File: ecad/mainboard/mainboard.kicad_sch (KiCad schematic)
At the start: 29 parts, among them M1 Left Motor, M2 Right Motor, Q1 IRLB8721PBF, Q2 IRLB8721PBF, U1 LM339

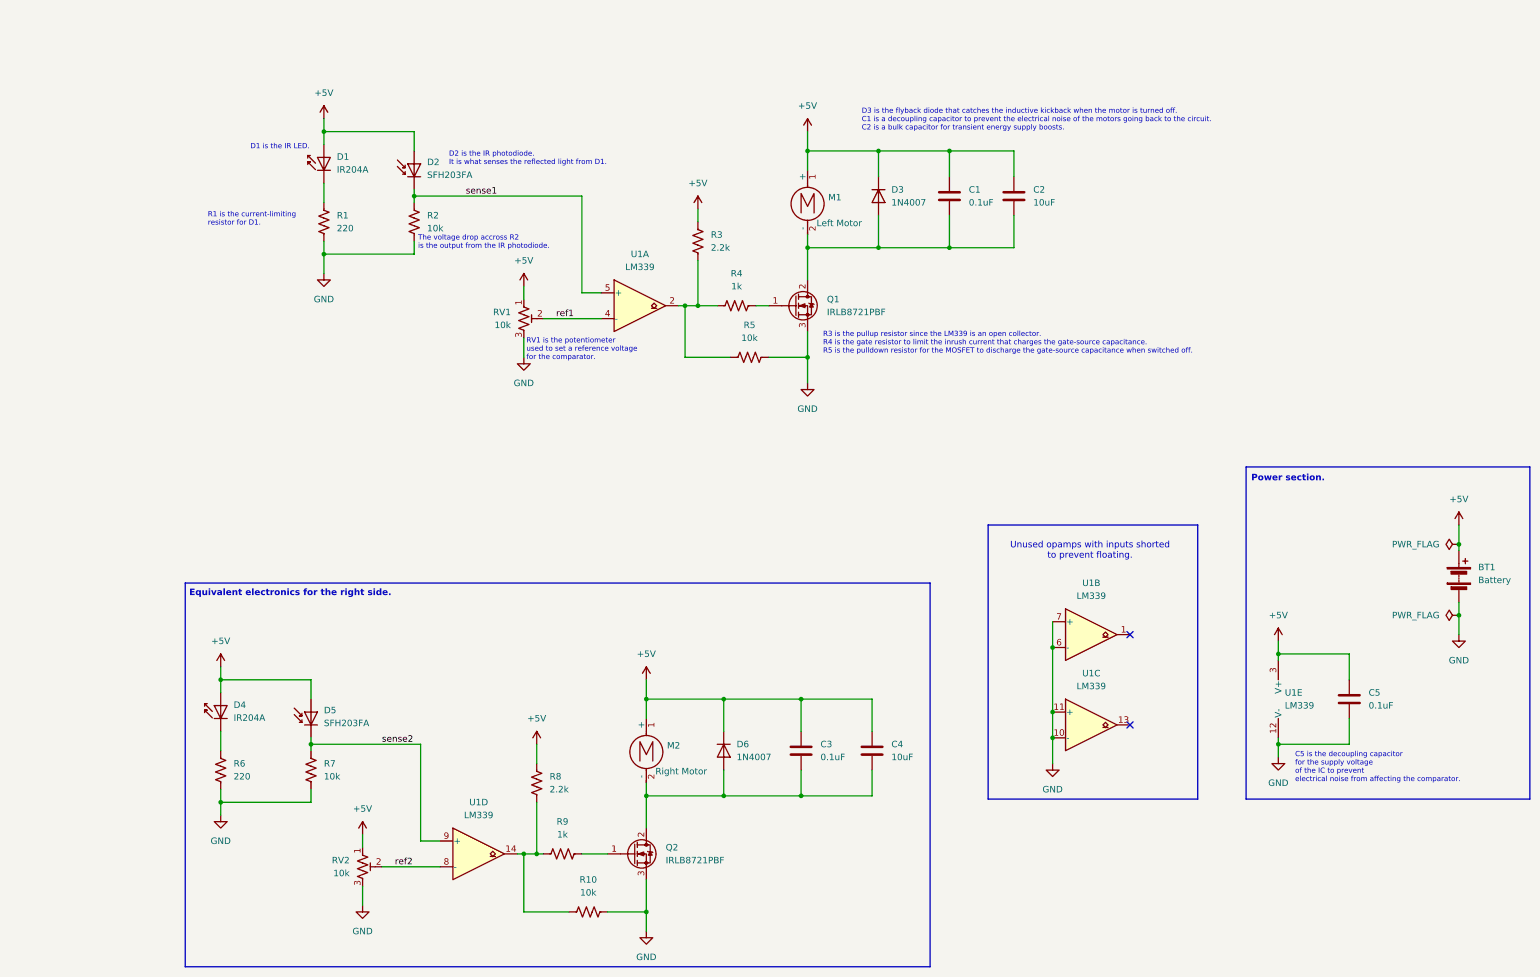
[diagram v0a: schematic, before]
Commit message: update schematics with smd components
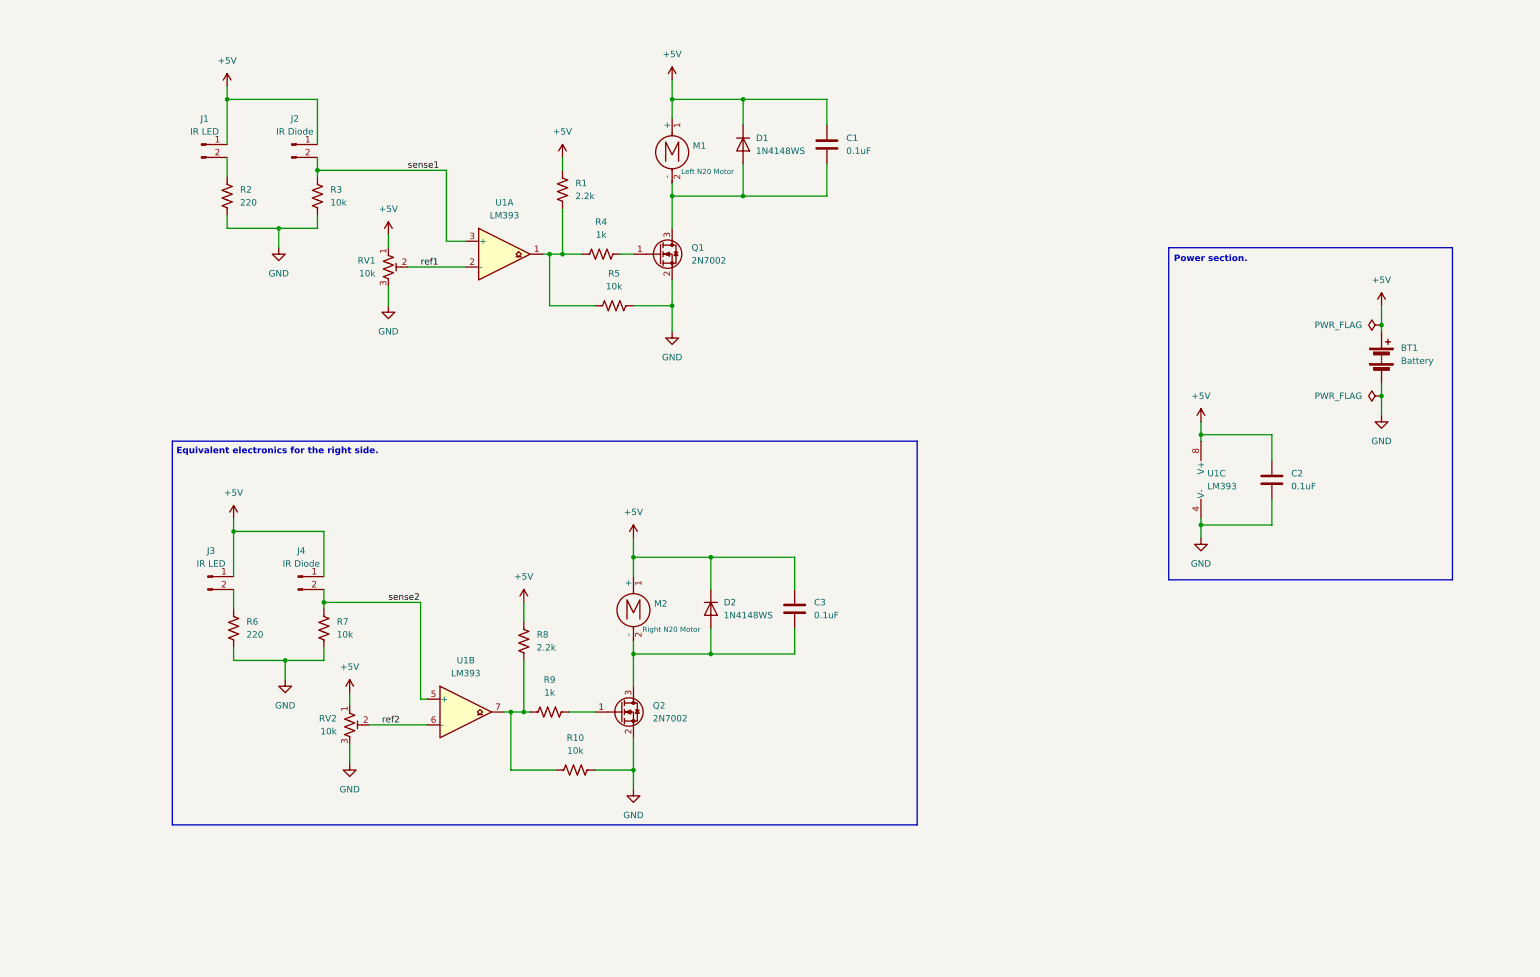
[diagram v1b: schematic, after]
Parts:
- removed C2, C4: 10uF, symbol Device:C
- removed D1, D4: IR204A, LED_THT:LED_D3.0mm_IRBlack, symbol LED:IR204A
- removed D2, D5: SFH203FA, LED_THT:LED_D5.0mm_IRGrey, symbol Sensor_Optical:SFH203FA
- removed Q1, Q2: IRLB8721PBF, Package_TO_SOT_THT:TO-220-3_Vertical, symbol Transistor_FET:IRLB8721PBF
- removed U1: LM339, symbol Comparator:LM339
- added J1, J3: IR LED, Connector_JST:JST_XH_S2B-XH-A_1x02_P2.50mm_Horizontal, symbol Connector:Conn_01x02_Pin
- added J2, J4: IR Diode, Connector_JST:JST_XH_S2B-XH-A_1x02_P2.50mm_Horizontal, symbol Connector:Conn_01x02_Pin
- added Q1, Q2: 2N7002, Package_TO_SOT_SMD:SOT-23, symbol Transistor_FET:2N7002
- added U1: LM393, Package_SO:SOIC-8_3.9x4.9mm_P1.27mm, symbol Comparator:LM393
- C1, C3: footprint (none) -> Capacitor_SMD:C_0402_1005Metric
- C2: renamed from C5; footprint (none) -> Capacitor_SMD:C_0402_1005Metric
- D1: renamed from D3; value 1N4007 -> 1N4148WS; footprint Diode_THT:D_DO-41_SOD81_P10.16mm_Horizontal -> Diode_SMD:D_SOD-323; symbol Diode:1N4007 -> Diode:1N4148WS
- D2: renamed from D6; value 1N4007 -> 1N4148WS; footprint Diode_THT:D_DO-41_SOD81_P10.16mm_Horizontal -> Diode_SMD:D_SOD-323; symbol Diode:1N4007 -> Diode:1N4148WS
- M1: value Left Motor -> Left N20 Motor; footprint Connector_PinHeader_2.54mm:PinHeader_1x02_P2.54mm_Vertical -> Connector_JST:JST_ZH_B2B-ZR_1x02_P1.50mm_Vertical
- M2: value Right Motor -> Right N20 Motor; footprint Connector_PinHeader_2.54mm:PinHeader_1x02_P2.54mm_Vertical -> Connector_JST:JST_ZH_B2B-ZR_1x02_P1.50mm_Vertical
- R1: renamed from R3; footprint Resistor_THT:R_Axial_DIN0309_L9.0mm_D3.2mm_P2.54mm_Vertical -> Resistor_SMD:R_0603_1608Metric
- R10, R4, R5, R6, R7, R8, R9: footprint Resistor_THT:R_Axial_DIN0309_L9.0mm_D3.2mm_P2.54mm_Vertical -> Resistor_SMD:R_0603_1608Metric
- R2: renamed from R1; footprint Resistor_THT:R_Axial_DIN0309_L9.0mm_D3.2mm_P2.54mm_Vertical -> Resistor_SMD:R_0603_1608Metric
- R3: renamed from R2; footprint Resistor_THT:R_Axial_DIN0309_L9.0mm_D3.2mm_P2.54mm_Vertical -> Resistor_SMD:R_0603_1608Metric
- RV1, RV2: footprint Potentiometer_SMD:Potentiometer_Bourns_3214J_Horizontal -> Potentiometer_THT:Potentiometer_Bourns_3296W_Vertical
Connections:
- net +5V: now also J1.1 (Pin_1), J2.1 (Pin_1), J3.1 (Pin_1), J4.1 (Pin_1), U1.8 (V+)
- net GND: now also Q1.2 (S), Q2.2 (S), U1.4 (V-)
- net ref1: now also U1.2 (-)
- net ref2: now also U1.6 (-)
- net sense1: now also J2.2 (Pin_2), U1.3 (+)
- net sense2: now also J4.2 (Pin_2), U1.5 (+)
- net at C3.2, D2.2 (A), M2.2 (-): now also Q2.3 (D)
- net at R1.1, R4.1, R5.1: now also U1.1
- net at R6.1: now also J3.2 (Pin_2)
- net at C1.2, D1.2 (A), M1.2 (-): now also Q1.3 (D)
- net at R10.1, R8.1, R9.1: now also U1.7
- net at R4.2: now also Q1.1 (G)
- net at R9.2: now also Q2.1 (G)
- net at R2.1: now also J1.2 (Pin_2)
- no-connect marks 2 -> 0
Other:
- note removed: "C5 is the decoupling capacitor for the supply voltage of the IC to prevent electrical noise from affecting the comparator."
- note removed: "D1 is the IR LED."
- note removed: "D2 is the IR photodiode. It is what senses the reflected light from D1."
- note removed: "D3 is the flyback diode that catches the inductive kickback when the motor is turned off. C1 is a decoupling capacitor to prevent the electrical noise of the motors going back to the circuit. C2 is a bulk capacitor for transient energy supply boosts."
- note removed: "R1 is the current-limiting resistor for D1."
- note removed: "R3 is the pullup resistor since the LM339 is an open collector. R4 is the gate resistor to limit the inrush current that charges the gate-source capacitance. R5 is the pulldown resistor for the MOSFET to discharge the gate-source capacitance when switched off."
- note removed: "RV1 is the potentiometer used to set a reference voltage for the comparator."
- note removed: "The voltage drop accross R2 is the output from the IR photodiode."
- note removed: "Unused opamps with inputs shorted to prevent floating."
- moved on the sheet: BT1, C1, C2, C3, D1, D2, M1, R1, R10, R2, R3, R4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

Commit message: change operating voltage to 3.3v and add connector for regulator
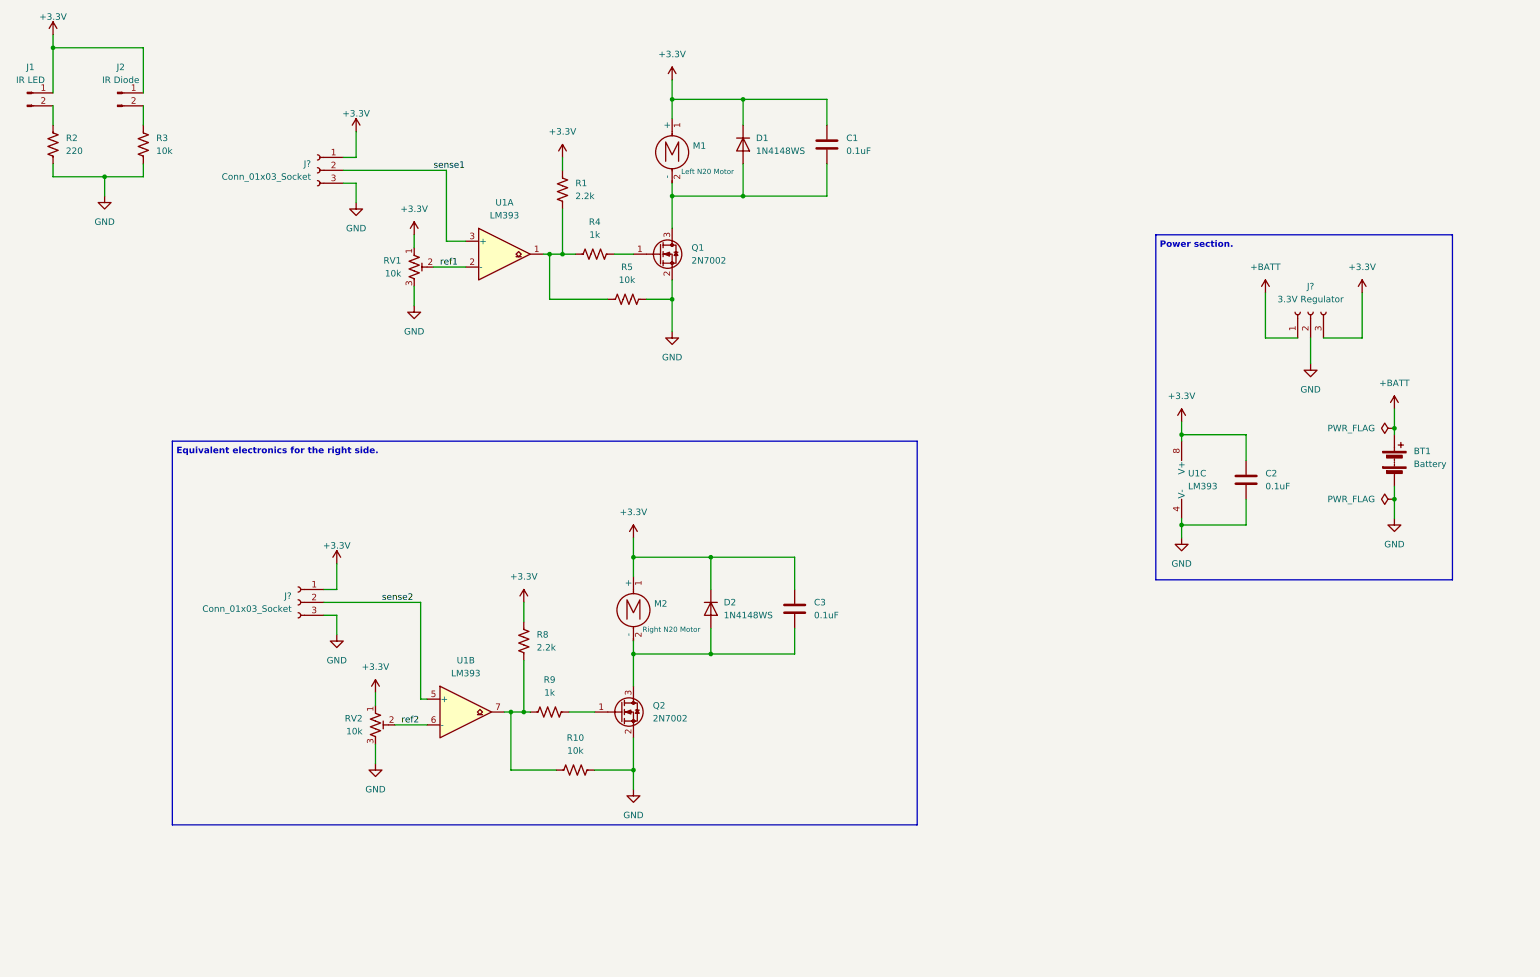
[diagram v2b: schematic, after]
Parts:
- removed J3: IR LED, Connector_JST:JST_XH_S2B-XH-A_1x02_P2.50mm_Horizontal, symbol Connector:Conn_01x02_Pin
- removed J4: IR Diode, Connector_JST:JST_XH_S2B-XH-A_1x02_P2.50mm_Horizontal, symbol Connector:Conn_01x02_Pin
- removed R6: 220, Resistor_SMD:R_0603_1608Metric, symbol Device:R_US
- removed R7: 10k, Resistor_SMD:R_0603_1608Metric, symbol Device:R_US
- added J?: 3.3V Regulator, symbol Connector:Conn_01x03_Socket
- added J? (x2): Conn_01x03_Socket, symbol Connector:Conn_01x03_Socket
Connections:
- net GND: now also J?.2 (Pin_2), J?.3 (Pin_3), J?.3 (Pin_3)
- net sense1: now also J?.2 (Pin_2); no longer J2.2 (Pin_2), R3.1
- net sense2: now also J?.2 (Pin_2)
- net +5V renamed +3.3V
- net +3.3V: now also J?.1 (Pin_1), J?.1 (Pin_1), J?.3 (Pin_3); no longer BT1.1 (+)
- new net: J2.2 (Pin_2), R3.1
- new net +BATT: BT1.1 (+), J?.1 (Pin_1)
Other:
- moved on the sheet: BT1, C2, J1, J2, R2, R3, R4, R5, RV1, RV2, U1C

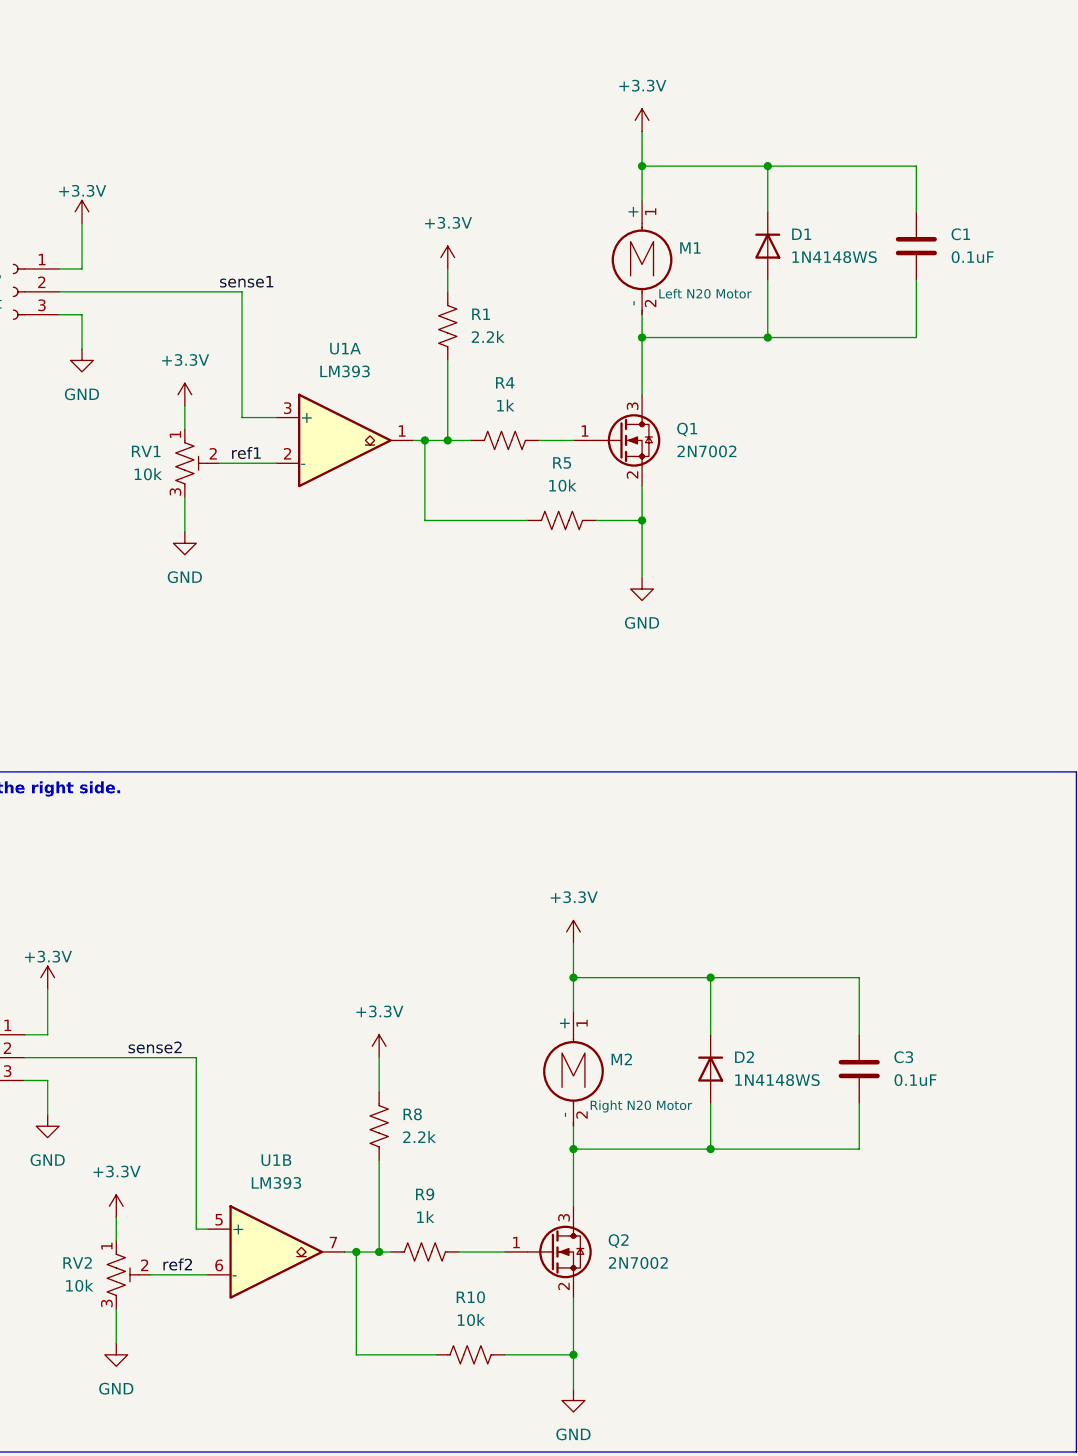
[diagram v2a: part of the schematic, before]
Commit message: ecad: replace diode and mosfet with tht parts
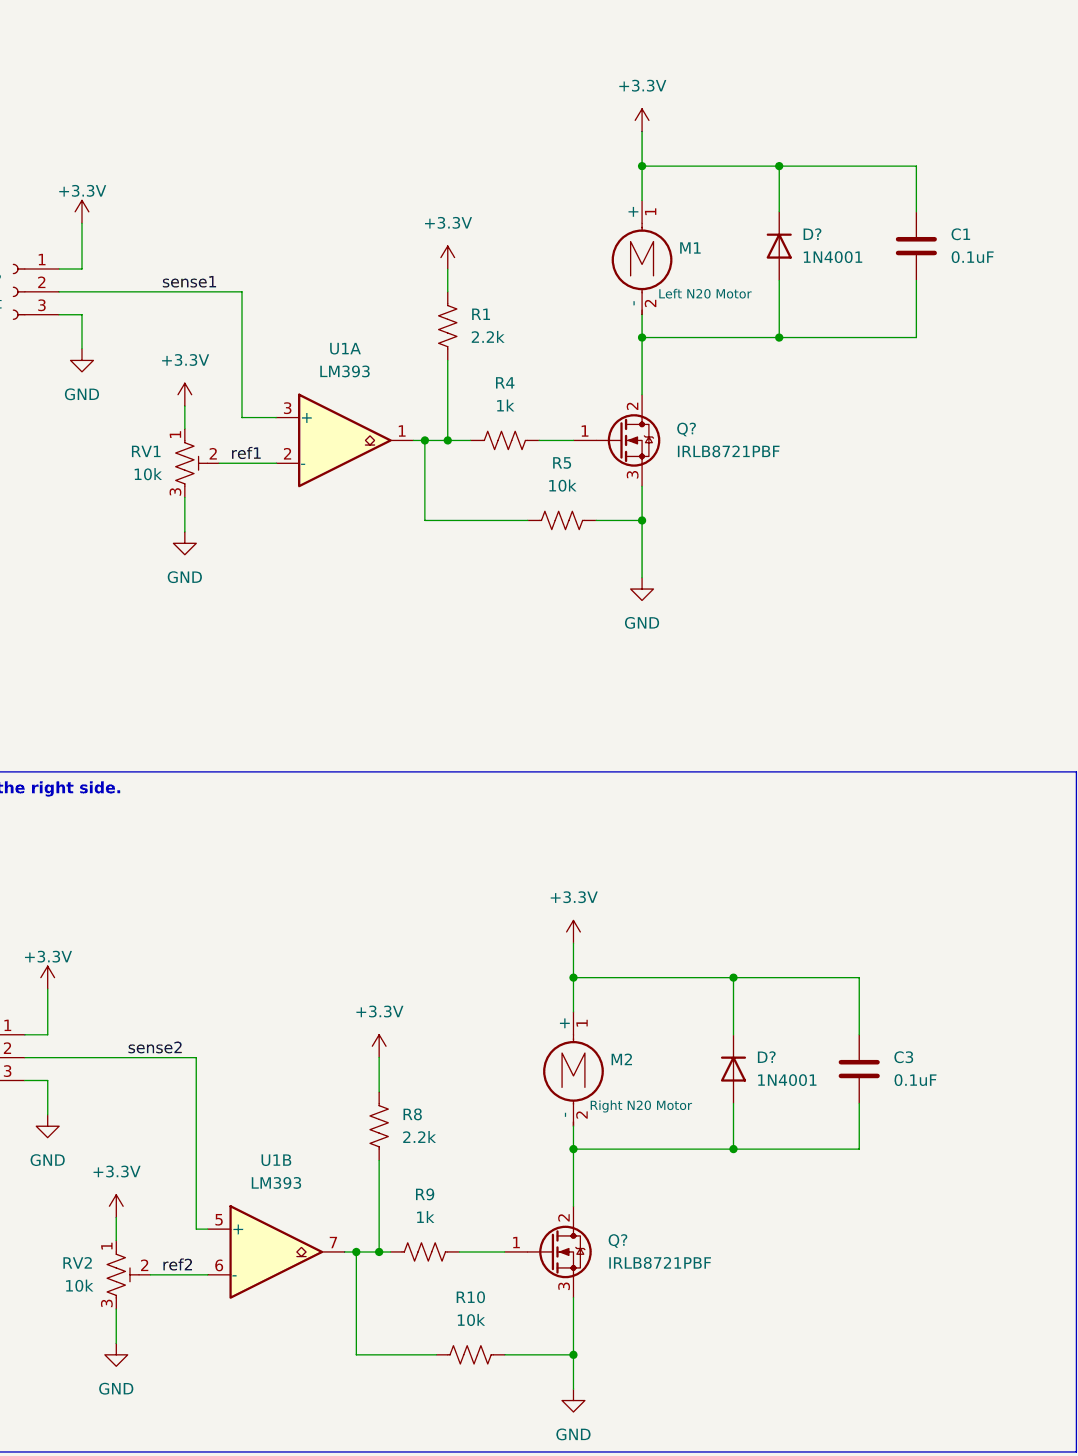
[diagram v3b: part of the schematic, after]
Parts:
- removed D1, D2: 1N4148WS, Diode_SMD:D_SOD-323, symbol Diode:1N4148WS
- removed Q1, Q2: 2N7002, Package_TO_SOT_SMD:SOT-23, symbol Transistor_FET:2N7002
- added D? (x2): 1N4001, Diode_THT:D_DO-41_SOD81_P10.16mm_Horizontal, symbol Diode:1N4001
- added Q? (x2): IRLB8721PBF, Package_TO_SOT_THT:TO-220-3_Vertical, symbol Transistor_FET:IRLB8721PBF
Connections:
- net +3.3V: now also D?.1 (K), D?.1 (K)
- net GND: now also Q?.3 (S), Q?.3 (S)
- net at R4.2: now also Q?.1 (G)
- net at C1.2, M1.2 (-): now also D?.2 (A), Q?.2 (D)
- net at R9.2: now also Q?.1 (G)
- net at C3.2, M2.2 (-): now also D?.2 (A), Q?.2 (D)
